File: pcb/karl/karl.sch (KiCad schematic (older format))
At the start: 8 parts, among them J1 Raspberry_Pi, J2 Power, J3 Battery, J4 LIDAR_Power, J5 Motor_Power, U1 MCP3421A0T-ECH

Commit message: project saved
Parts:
- U1: footprint (none) -> Package_TO_SOT_SMD:SOT-23-6
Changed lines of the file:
@@
 F 0 "U1" H 5800 7531 50  0000 C CNN
 F 1 "MCP3421A0T-ECH" H 5800 7440 50  0000 C CNN
-F 2 "" H 5800 6950 50  0001 C CIN
+F 2 "Package_TO_SOT_SMD:SOT-23-6" H 5800 6950 50  0001 C CIN
 F 3 "http://ww1.microchip.com/downloads/en/DeviceDoc/22003e.pdf" H 5800 6950 50  0001 C CNN
 F 4 "C29454" H 5800 6950 50  0001 C CNN "LCSC"

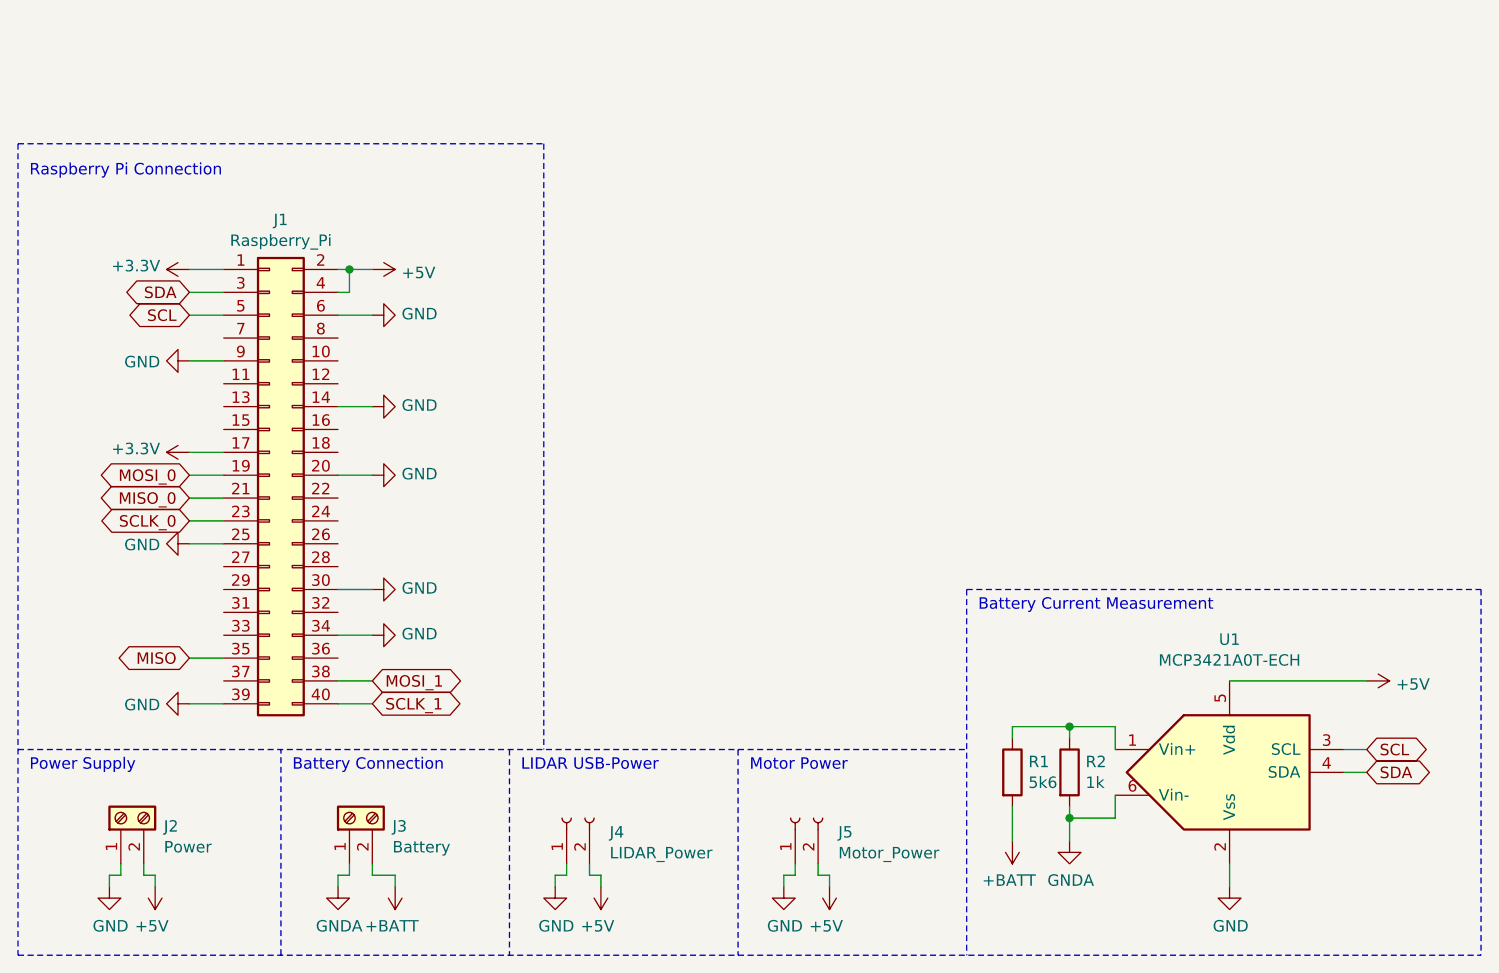
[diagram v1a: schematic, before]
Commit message: added turning lights
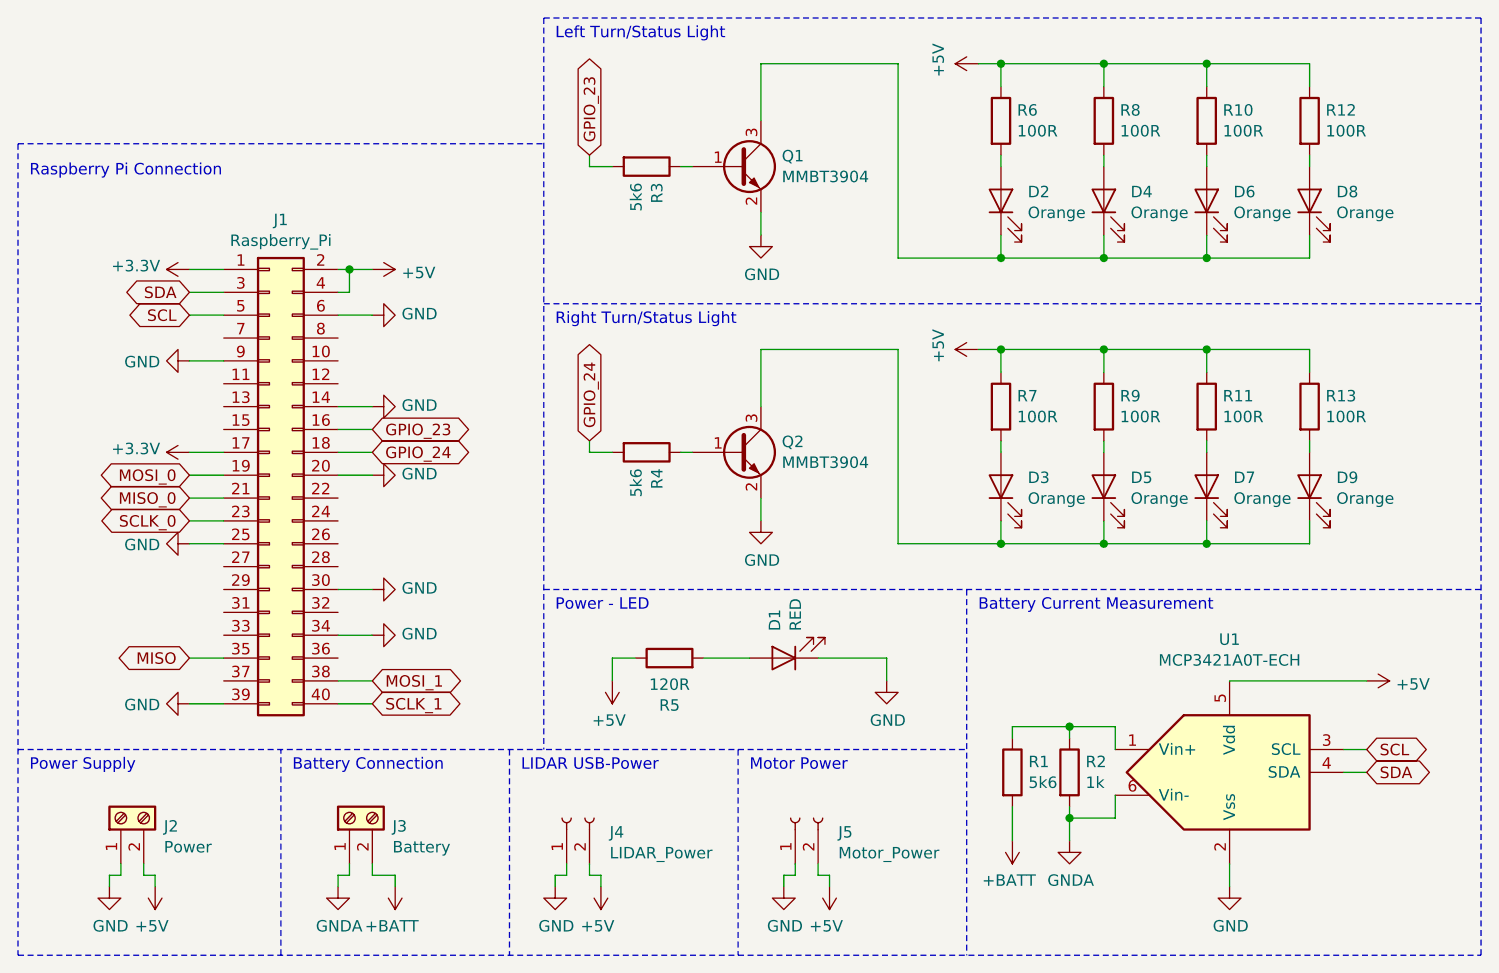
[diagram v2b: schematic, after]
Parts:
- added D1: RED, LED_SMD:LED_0603_1608Metric, symbol Device:LED
- added D2, D3, D4, D5, D6, D7, D8, D9: Orange, LED_SMD:LED_0603_1608Metric, symbol Device:LED
- added Q1, Q2: MMBT3904, Package_TO_SOT_SMD:SOT-23, symbol Transistor_BJT:MMBT3904
- added R10, R11, R12, R13, R6, R7, R8, R9: 100R, Resistor_SMD:R_0603_1608Metric, symbol Device:R
- added R3, R4: 5k6, Resistor_SMD:R_0603_1608Metric, symbol Device:R
- added R5: 120R, Resistor_SMD:R_0603_1608Metric, symbol Device:R
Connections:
- net +5V: now also R10.1, R11.1, R12.1, R13.1, R5.1, R6.1, R7.1, R8.1, R9.1
- net GND: now also D1.1 (K), Q1.2 (E), Q2.2 (E)
- net GPIO_23: now reaches J1.16 (Pin_16)
- net GPIO_23: now also R3.2
- net GPIO_24: now reaches J1.18 (Pin_18)
- net GPIO_24: now also R4.2
- new net: D1.2 (A), R5.2
- new net: Q2.1 (B), R4.1
- new net: D3.1 (K), D5.1 (K), D7.1 (K), D9.1 (K), Q2.3 (C)
- new net: D5.2 (A), R9.2
- new net: D3.2 (A), R7.2
- new net: D7.2 (A), R11.2
- new net: D9.2 (A), R13.2
- new net: Q1.1 (B), R3.1
- new net: D2.1 (K), D4.1 (K), D6.1 (K), D8.1 (K), Q1.3 (C)
- new net: D4.2 (A), R8.2
- new net: D2.2 (A), R6.2
- new net: D6.2 (A), R10.2
- new net: D8.2 (A), R12.2
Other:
- note added: "Left Turn/Status Light"
- note added: "Power - LED"
- note added: "Right Turn/Status Light"
